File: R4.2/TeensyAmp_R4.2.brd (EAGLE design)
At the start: 104 x 40 mm, 82 parts, among them IC5 NCP164CSN330T1G, IC6 PCM1865DBT, IC7 PCM1865DBT

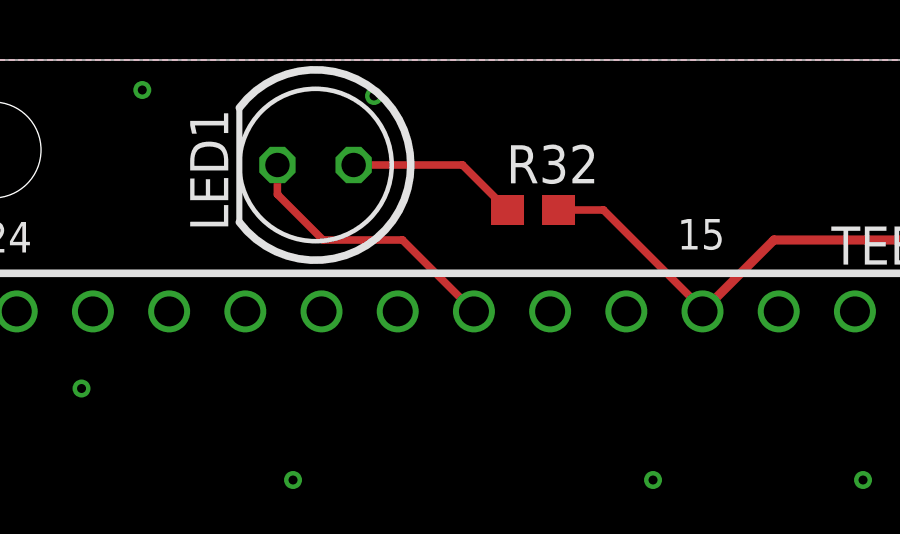
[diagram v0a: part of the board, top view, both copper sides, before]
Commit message: [R4.2] LED pin on 27
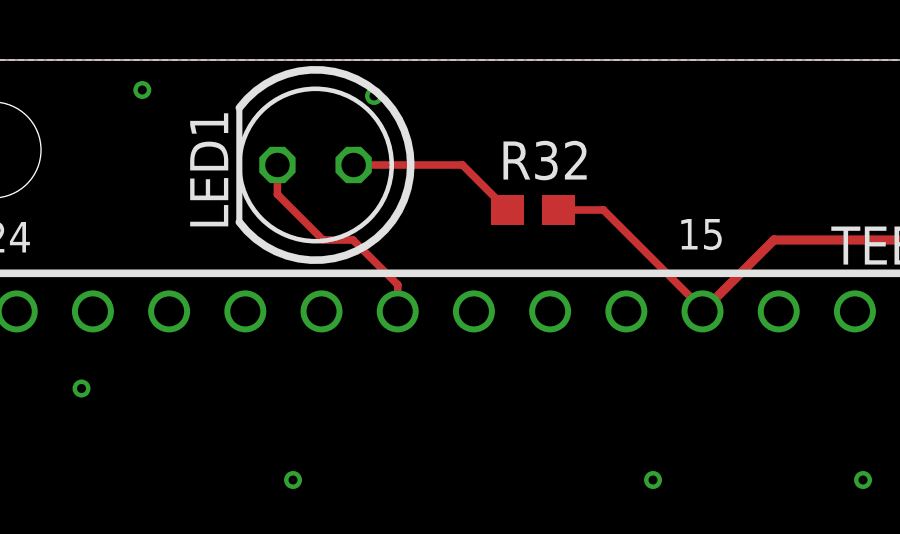
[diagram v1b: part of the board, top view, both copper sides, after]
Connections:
- new net LED2: LED1.K, TEENSY4.1.19
- net LED: no longer LED1.K
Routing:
- net LED: track 9.15 -> 0.00 mm
- net LED2: track 0.00 -> 7.13 mm
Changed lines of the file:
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@@
 </element>
 <element name="R28" library="jlm_resistors" library_urn="urn:adsk.eagle:library:22393478" package="R0603" package3d_urn="urn:adsk.eagle:package:16649223/2" value="4,7k" x="57.125" y="12.875" smashed="yes" rot="R90">
-<attribute name="NAME" x="56.236" y="11.236" size="1.27" layer="25" rot="R90"/>
+<attribute name="NAME" x="56.236" y="11.236" size="1.27" layer="25" font="vector" rot="R90"/>
 <attribute name="VALUE" x="57.657" y="11.486" size="1.016" layer="27" font="vector" ratio="20" rot="R90"/>
 </element>
 <element name="R27" library="jlm_resistors" library_urn="urn:adsk.eagle:library:22393478" package="R0603" package3d_urn="urn:adsk.eagle:package:16649223/2" value="4,7k" x="60.625" y="12.75" smashed="yes" rot="R90">
-<attribute name="NAME" x="59.736" y="11.236" size="1.27" layer="25" rot="R90"/>
+<attribute name="NAME" x="59.736" y="11.236" size="1.27" layer="25" font="vector" rot="R90"/>
 <attribute name="VALUE" x="61.157" y="11.361" size="1.016" layer="27" font="vector" ratio="20" rot="R90"/>
 </element>
 <element name="C36" library="jlm_cap" library_urn="urn:adsk.eagle:library:29887427" package="C0805" package3d_urn="urn:adsk.eagle:package:16649544/2" value="10µ" x="61.875" y="4.875" smashed="yes" rot="R270">
-<attribute name="NAME" x="63.145" y="6.145" size="1.27" layer="25" rot="R270"/>
+<attribute name="NAME" x="63.145" y="6.145" size="1.27" layer="25" font="vector" rot="R270"/>
 <attribute name="VALUE" x="62.29" y="3.605" size="1.016" layer="27" font="vector" ratio="20" rot="R90"/>
 </element>
 <element name="C35" library="jlm_cap" library_urn="urn:adsk.eagle:library:29887427" package="C0805" package3d_urn="urn:adsk.eagle:package:16649544/2" value="10µ" x="66" y="4.875" smashed="yes" rot="R270">
-<attribute name="NAME" x="67.27" y="6.145" size="1.27" layer="25" rot="R270"/>
+<attribute name="NAME" x="67.27" y="6.145" size="1.27" layer="25" font="vector" rot="R270"/>
 <attribute name="VALUE" x="66.415" y="3.605" size="1.016" layer="27" font="vector" ratio="20" rot="R90"/>
 </element>
 <element name="L1" library="jlm_inductor" library_urn="urn:adsk.eagle:library:25120685" package="R0805" package3d_urn="urn:adsk.eagle:package:16649225/2" value="BLM" x="64" y="8" smashed="yes" rot="R180">
-<attribute name="NAME" x="64.365" y="9.27" size="1.27" layer="25"/>
+<attribute name="NAME" x="64.365" y="9.27" size="1.27" layer="25" font="vector"/>
 <attribute name="VALUE" x="64.635" y="10.54" size="1.27" layer="27" rot="R180"/>
 </element>
@@
 <attribute name="MF" value="" x="47" y="-12" size="1.778" layer="27" display="off"/>
 <attribute name="MPN" value="" x="47" y="-12" size="1.778" layer="27" display="off"/>
-<attribute name="NAME" x="36.645" y="1.1425" size="1.27" layer="25" rot="R90"/>
+<attribute name="NAME" x="36.645" y="1.1425" size="1.27" layer="25" font="vector" rot="R90"/>
 <attribute name="OC_FARNELL" value="unknown" x="47" y="-12" size="1.778" layer="27" display="off"/>
 <attribute name="OC_NEWARK" value="unknown" x="47" y="-12" size="1.778" layer="27" display="off"/>
@@
 </element>
 <element name="D1" library="jlm_diode" library_urn="urn:adsk.eagle:library:29780204" package="SOD123" package3d_urn="urn:adsk.eagle:package:43420/1" value="SMF6V0TFTR" x="58" y="6" smashed="yes" rot="R270">
-<attribute name="NAME" x="59" y="7.1" size="1.27" layer="25" rot="R270"/>
+<attribute name="NAME" x="59" y="7.1" size="1.27" layer="25" font="vector" rot="R270"/>
 <attribute name="OC_FARNELL" value="2989529" x="45" y="6" size="1.778" layer="27" rot="R270" display="off"/>
 <attribute name="POPULARITY" value="22" x="45" y="6" size="1.778" layer="27" rot="R270" display="off"/>
@@
 </element>
 <element name="R29" library="jlm_resistors" library_urn="urn:adsk.eagle:library:22393478" package="R0603" package3d_urn="urn:adsk.eagle:package:16649223/2" value="1k" x="42" y="13" smashed="yes" rot="R270">
-<attribute name="NAME" x="41.111" y="11.361" size="1.27" layer="25" rot="R90"/>
+<attribute name="NAME" x="41.111" y="11.361" size="1.27" layer="25" font="vector" rot="R90"/>
 <attribute name="VALUE" x="42.532" y="12.111" size="1.016" layer="27" font="vector" ratio="20" rot="R90"/>
 </element>
 <element name="R30" library="jlm_resistors" library_urn="urn:adsk.eagle:library:22393478" package="R0603" package3d_urn="urn:adsk.eagle:package:16649223/2" value="1k" x="38.375" y="13" smashed="yes" rot="R270">
-<attribute name="NAME" x="37.736" y="11.361" size="1.27" layer="25" rot="R90"/>
+<attribute name="NAME" x="37.736" y="11.361" size="1.27" layer="25" font="vector" rot="R90"/>
 <attribute name="VALUE" x="38.907" y="12.236" size="1.016" layer="27" font="vector" ratio="20" rot="R90"/>
 </element>
 <element name="LED1" library="jlm_optical" library_urn="urn:adsk.eagle:library:22393424" package="LED5MM" package3d_urn="urn:adsk.eagle:package:29506708/2" value="red" x="19.75" y="36.5" smashed="yes" rot="R180">
-<attribute name="NAME" x="16.8416" y="34.3" size="1.27" layer="25" ratio="10" rot="R90"/>
+<attribute name="NAME" x="16.8416" y="34.3" size="1.27" layer="25" font="vector" ratio="10" rot="R90"/>
 <attribute name="VALUE" x="18.7004" y="35.9466" size="1.016" layer="27" font="vector" ratio="20"/>
 </element>
 <element name="R32" library="jlm_resistors" library_urn="urn:adsk.eagle:library:22393478" package="R0603" package3d_urn="urn:adsk.eagle:package:16649223/2" value="330" x="27" y="35" smashed="yes">
-<attribute name="NAME" x="26.111" y="35.889" size="1.27" layer="25"/>
+<attribute name="NAME" x="25.861" y="36.014" size="1.27" layer="25" font="vector"/>
 <attribute name="VALUE" x="25.736" y="34.468" size="1.016" layer="27" font="vector" ratio="20"/>
 </element>
@@
 <signal name="LED">
 <contactref element="TEENSY4.1" pad="18"/>
-<contactref element="LED1" pad="K"/>
-<wire x1="25.03" y1="31.62" x2="22.65" y2="34" width="0.254" layer="1"/>
-<wire x1="22.65" y1="34" x2="20" y2="34" width="0.254" layer="1"/>
-<wire x1="20" y1="34" x2="18.48" y2="35.52" width="0.254" layer="1"/>
-<wire x1="18.48" y1="35.52" x2="18.48" y2="36.5" width="0.254" layer="1"/>
 </signal>
 <signal name="N$72">
@@
 <wire x1="24.65" y1="36.5" x2="26.15" y2="35" width="0.254" layer="1"/>
 </signal>
+<signal name="LED2">
+<contactref element="TEENSY4.1" pad="19"/>
+<contactref element="LED1" pad="K"/>
+<wire x1="18.48" y1="36.5" x2="18.48" y2="35.52" width="0.254" layer="1"/>
+<wire x1="20" y1="34" x2="21" y2="34" width="0.254" layer="1"/>
+<wire x1="21" y1="34" x2="22.49" y2="32.51" width="0.254" layer="1"/>
+<wire x1="22.49" y1="32.51" x2="22.49" y2="31.62" width="0.254" layer="1"/>
+<wire x1="18.48" y1="35.52" x2="20" y2="34" width="0.254" layer="1"/>
+</signal>
 </signals>
